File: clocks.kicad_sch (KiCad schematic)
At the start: 17 parts, among them U42 CDCE906PWR, Y5 ABM8G-12.000MHZ-18-D2Y-T, Y6 AX3DCF1-200.0000

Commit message: Loclib
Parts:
- C365, C367: footprint antmicro-footprints:0402-cap -> K410T-devboard-footprints:0402-cap; symbol antmicroCapacitors0402:C_22p_0402 -> K410T-devboard:C_22p_0402
- C366, C373: footprint antmicro-footprints:0201-cap -> K410T-devboard-footprints:0201-cap; symbol antmicroCapacitorsmisc:C_4u7_0201 -> K410T-devboard:C_4u7_0201
- C368, C369, C370, C371, C372: footprint antmicro-footprints:0402-cap -> K410T-devboard-footprints:0402-cap; symbol antmicroCapacitors0402:C_100n_0402 -> K410T-devboard:C_100n_0402
- R334: footprint antmicro-footprints:0402-res -> K410T-devboard-footprints:0402-res; symbol antmicroResistors0402:R_100R_0402 -> K410T-devboard:R_100R_0402
- R335, R336, R337: footprint antmicro-footprints:0402-res -> K410T-devboard-footprints:0402-res; symbol antmicroResistors0402:R_22R_0402 -> K410T-devboard:R_22R_0402
- R352: footprint antmicro-footprints:0402-res -> K410T-devboard-footprints:0402-res; symbol antmicroResistors0402:R_10k_0402 -> K410T-devboard:R_10k_0402
- U42: footprint antmicro-footprints:TSSOP-20_W4.4mm -> K410T-devboard-footprints:TSSOP-20_W4.4mm; symbol antmicroClockTimingClockGeneratorsPLLsFrequencySynthesizers:CDCE906PWR -> K410T-devboard:CDCE906PWR
- Y5: footprint antmicro-footprints:KX-7 -> K410T-devboard-footprints:KX-7; symbol antmicroCrystals:ABM8G-12.000MHZ-18-D2Y-T -> K410T-devboard:ABM8G-12.000MHZ-18-D2Y-T
- Y6: footprint antmicro-footprints:AX3DAF1 -> K410T-devboard-footprints:AX3DAF1; symbol antmicroOscillators:AX3DCF1-200.0000 -> K410T-devboard:AX3DCF1-200.0000

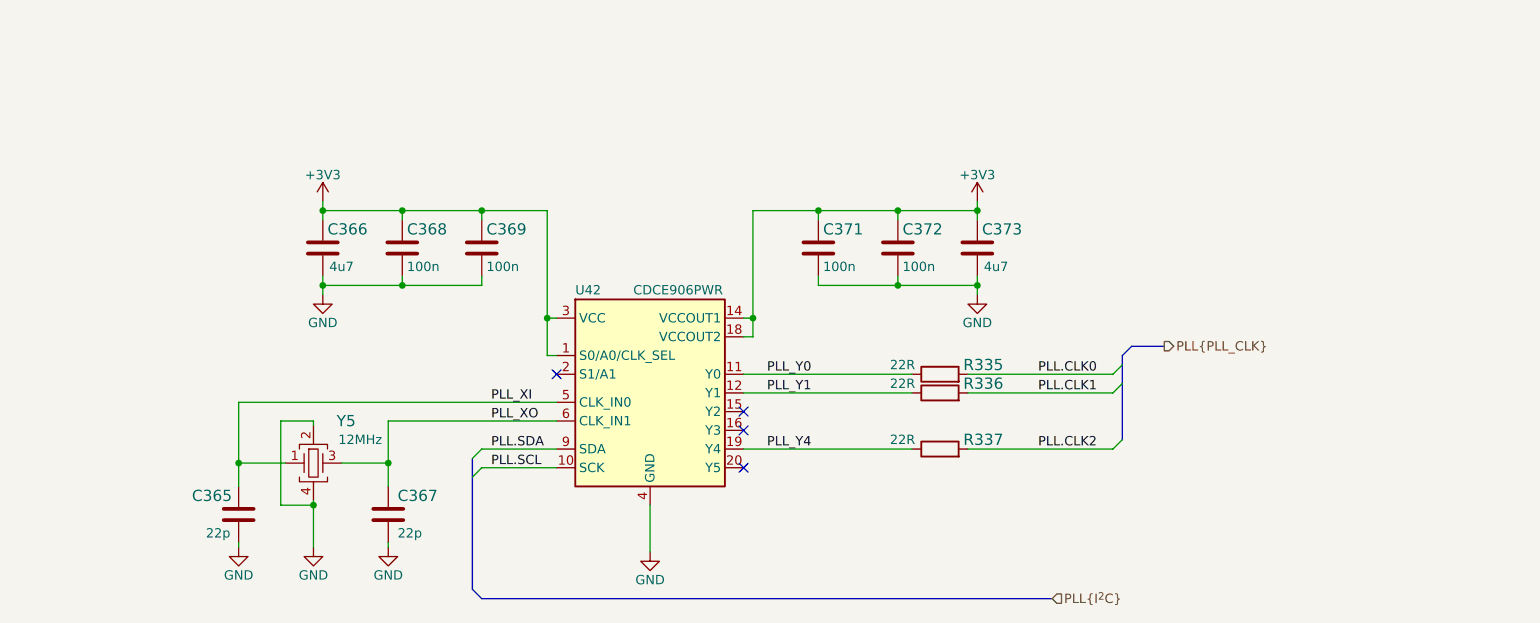
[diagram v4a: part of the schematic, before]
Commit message: Corrected schematic according to review
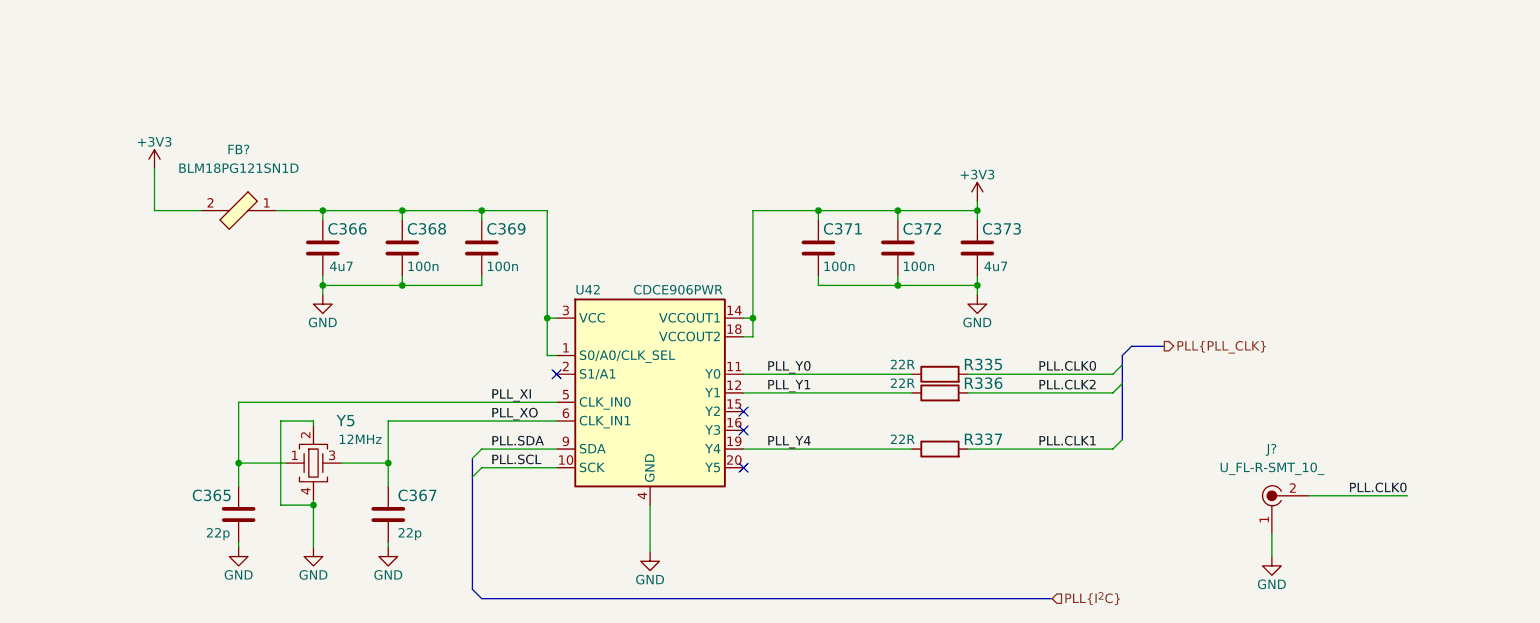
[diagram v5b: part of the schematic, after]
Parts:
- added FB?: BLM18PG121SN1D, K410T-devboard-footprints:0603-res, symbol K410T-devboard:BLM18PG121SN1D
- added J?: U_FL-R-SMT_10_, antmicro-footprints:Coax_Conn_U.FL, symbol antmicroCoaxialConnectorsRF:U_FL-R-SMT_10_
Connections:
- net +3V3: now also FB?.2; no longer C366.1, C368.1, C369.1, U42.1 (S0/A0/CLK_SEL), U42.3 (VCC), U42.7 (VCC)
- net GND: now also J?.1
- net PLL.CLK0: now also J?.2
- net PLL.CLK1: now also R337.2; no longer R336.2
- net PLL.CLK2: now also R336.2; no longer R337.2
- new net: C366.1, C368.1, C369.1, FB?.1, U42.1 (S0/A0/CLK_SEL), U42.3 (VCC), U42.7 (VCC)
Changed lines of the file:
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@@
     (rev "0.0.99")
   )
+  (bus_alias "CLK" (members "CLK_P" "CLK_N"))
+  (bus_alias "I^{2}C" (members "SDA" "SCL"))
   (bus_alias "PLL_CLK" (members "CLK[0..2]"))
-  (bus_alias "I^{2}C" (members "SDA" "SCL"))
-  (bus_alias "CLK" (members "CLK_P" "CLK_N"))
+  (junction (at 176.53 175.895) (diameter 0) (color 0 0 0 0)
+  )
   (junction (at 265.43 175.895) (diameter 0) (color 0 0 0 0)
   )
@@
   )
   (junction (at 254.635 186.055) (diameter 0) (color 0 0 0 0)
-  )
-  (junction (at 176.53 175.895) (diameter 0) (color 0 0 0 0)
   )
   (junction (at 200.025 78.74) (diameter 0) (color 0 0 0 0)
@@
     (stroke (width 0) (type default) (color 0 0 0 0))
   )
+  (wire (pts (xy 305.435 219.71) (xy 305.435 222.885))
+    (stroke (width 0) (type default) (color 0 0 0 0))
+  )
   (wire (pts (xy 265.43 186.055) (xy 254.635 186.055))
     (stroke (width 0) (type default) (color 0 0 0 0))
@@
     (stroke (width 0) (type default) (color 0 0 0 0))
   )
+  (wire (pts (xy 153.67 175.895) (xy 153.67 170.18))
+    (stroke (width 0) (type default) (color 0 0 0 0))
+  )
   (wire (pts (xy 232.41 82.55) (xy 233.68 82.55))
     (stroke (width 0) (type default) (color 0 0 0 0))
@@
     (stroke (width 0) (type default) (color 0 0 0 0))
   )
-  (wire (pts (xy 176.53 177.165) (xy 176.53 175.895))
+  (wire (pts (xy 310.515 214.63) (xy 323.85 214.63))
     (stroke (width 0) (type default) (color 0 0 0 0))
   )
@@
     (stroke (width 0) (type default) (color 0 0 0 0))
   )
+  (wire (pts (xy 160.02 175.895) (xy 153.67 175.895))
+    (stroke (width 0) (type default) (color 0 0 0 0))
+  )
   (wire (pts (xy 231.14 81.28) (xy 232.41 81.28))
     (stroke (width 0) (type default) (color 0 0 0 0))
@@
     (stroke (width 0) (type default) (color 0 0 0 0))
   )
+  (wire (pts (xy 176.53 175.895) (xy 176.53 177.165))
+    (stroke (width 0) (type default) (color 0 0 0 0))
+  )
   (wire (pts (xy 265.43 186.055) (xy 265.43 187.325))
     (stroke (width 0) (type default) (color 0 0 0 0))
@@
     (stroke (width 0) (type default) (color 0 0 0 0))
   )
-  (wire (pts (xy 176.53 174.625) (xy 176.53 175.895))
-    (stroke (width 0) (type default) (color 0 0 0 0))
-  )
   (wire (pts (xy 242.57 82.55) (xy 242.57 78.74))
     (stroke (width 0) (type default) (color 0 0 0 0))
@@
   )
   (wire (pts (xy 194.945 78.74) (xy 200.025 78.74))
+    (stroke (width 0) (type default) (color 0 0 0 0))
+  )
+  (wire (pts (xy 170.18 175.895) (xy 176.53 175.895))
     (stroke (width 0) (type default) (color 0 0 0 0))
   )
@@
     (effects (font (size 1.27 1.27)) (justify left bottom))
   )
-  (label "PLL.CLK2" (at 273.685 208.28 0)
+  (label "PLL.CLK2" (at 273.685 200.66 0)
     (effects (font (size 1.27 1.27)) (justify left bottom))
   )
@@
     (effects (font (size 1.27 1.27)) (justify left bottom))
   )
+  (label "PLL.CLK0" (at 323.85 214.63 180)
+    (effects (font (size 1.27 1.27)) (justify right bottom))
+  )
   (label "PLL_XO" (at 199.39 204.47 0)
     (effects (font (size 1.27 1.27)) (justify left bottom))
@@
     (effects (font (size 1.27 1.27)) (justify left bottom))
   )
-  (label "PLL.CLK1" (at 273.685 200.66 0)
+  (label "PLL.CLK1" (at 273.685 208.28 0)
     (effects (font (size 1.27 1.27)) (justify left bottom))
   )
@@
     (pin "1")
   )
-  (symbol (lib_id "K410T-devboard:+3V3") (at 176.53 174.625 0) (unit 1)
+  (symbol (lib_id "K410T-devboard:+3V3") (at 153.67 170.18 0) (unit 1)
     (in_bom yes) (on_board yes) (fields_autoplaced)
-    (property "Reference" "#PWR0411" (id 0) (at 176.53 178.435 0)
-      (effects (font (size 1.27 1.27)) hide)
-    )
-    (property "Value" "+3V3" (id 1) (at 176.53 171.0492 0))
-    (property "Footprint" "" (id 2) (at 176.53 174.625 0)
-      (effects (font (size 1.27 1.27)) hide)
-    )
-    (property "Datasheet" "" (id 3) (at 176.53 174.625 0)
+    (property "Reference" "#PWR0411" (id 0) (at 153.67 173.99 0)
+      (effects (font (size 1.27 1.27)) hide)
+    )
+    (property "Value" "+3V3" (id 1) (at 153.67 166.6042 0))
+    (property "Footprint" "" (id 2) (at 153.67 170.18 0)
+      (effects (font (size 1.27 1.27)) hide)
+    )
+    (property "Datasheet" "" (id 3) (at 153.67 170.18 0)
       (effects (font (size 1.27 1.27)) hide)
     )
@@
     (pin "2")
   )
+  (symbol (lib_id "antmicroCoaxialConnectorsRF:U_FL-R-SMT_10_") (at 305.435 214.63 0) (unit 1)
+    (in_bom yes) (on_board yes) (fields_autoplaced)
+    (property "Reference" "J?" (id 0) (at 305.4349 208.28 0))
+    (property "Value" "U_FL-R-SMT_10_" (id 1) (at 305.4349 210.82 0))
+    (property "Footprint" "antmicro-footprints:Coax_Conn_U.FL" (id 2) (at 310.515 209.55 0)
+      (effects (font (size 1.524 1.524)) (justify left) hide)
+    )
+    (property "Datasheet" "https://media.digikey.com/pdf/Data%20Sheets/Hirose%20PDFs/UFL%20Series.pdf" (id 3) (at 310.515 207.01 0)
+      (effects (font (size 1.524 1.524)) (justify left) hide)
+    )
+    (property "MPN" "U.FL-R-SMT(10)" (id 4) (at 310.515 201.93 0)
+      (effects (font (size 1.524 1.524)) (justify left) hide)
+    )
+    (property "Manufacturer" "Hirose Electric Co Ltd" (id 5) (at 310.515 186.69 0)
+      (effects (font (size 1.524 1.524)) (justify left) hide)
+    )
+    (pin "1")
+    (pin "2")
+  )
   (symbol (lib_id "K410T-devboard:ABM8G-12.000MHZ-18-D2Y-T ") (at 175.26 210.185 0) (unit 1)
     (in_bom yes) (on_board yes)
@@
     (pin "2")
   )
+  (symbol (lib_id "K410T-devboard:GND") (at 305.435 222.885 0) (unit 1)
+    (in_bom yes) (on_board yes)
+    (property "Reference" "#PWR?" (id 0) (at 305.435 229.235 0)
+      (effects (font (size 1.524 1.524)) hide)
+    )
+    (property "Value" "GND" (id 1) (at 305.435 226.695 0))
+    (property "Footprint" "" (id 2) (at 305.435 222.885 0)
+      (effects (font (size 1.27 1.27)) hide)
+    )
+    (property "Datasheet" "" (id 3) (at 305.435 222.885 0)
+      (effects (font (size 1.27 1.27)) hide)
+    )
+    (pin "1")
+  )
   (symbol (lib_id "K410T-devboard:+1V8") (at 201.93 60.325 0) (unit 1)
     (in_bom yes) (on_board yes) (fields_autoplaced)
@@
     (pin "1")
   )
+  (symbol (lib_id "K410T-devboard:BLM18PG121SN1D") (at 165.1 175.895 0) (mirror y) (unit 1)
+    (in_bom yes) (on_board yes) (fields_autoplaced)
+    (property "Reference" "FB?" (id 0) (at 165.1 167.64 0))
+    (property "Value" "BLM18PG121SN1D" (id 1) (at 165.1 170.18 0))
+    (property "Footprint" "K410T-devboard-footprints:0603-res" (id 2) (at 160.02 170.815 0)
+      (effects (font (size 1.27 1.27)) (justify left) hide)
+    )
+    (property "Datasheet" "https://www.murata.com/en-us/products/productdata/8796738650142/ENFA0003.pdf" (id 3) (at 160.02 168.275 0)
+      (effects (font (size 1.27 1.27)) (justify left) hide)
+    )
+    (property "MPN" "BLM18PG121SN1D" (id 4) (at 160.02 163.195 0)
+      (effects (font (size 1.27 1.27)) (justify left) hide)
+    )
+    (property "Manufacturer" "Murata Electronics North America" (id 5) (at 160.02 147.955 0)
+      (effects (font (size 1.27 1.27)) (justify left) hide)
+    )
+    (pin "1")
+    (pin "2")
+  )
   (symbol (lib_id "K410T-devboard:CDCE906PWR") (at 220.98 200.66 0) (unit 1)

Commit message: Finished implementing all changes from sch review
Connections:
- net at C366.1, C368.1, C369.1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: no longer U42.1 (S0/A0/CLK_SEL)
- new net SUP_MCU.PG_3V3: U42.1 (S0/A0/CLK_SEL)
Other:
- note removed: "Todo: -connect S0 to 3V3 PG ?"
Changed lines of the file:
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@@
   (junction (at 243.84 175.895) (diameter 0) (color 0 0 0 0)
-  )
-  (junction (at 207.01 190.5) (diameter 0) (color 0 0 0 0)
   )
   (junction (at 187.325 175.895) (diameter 0) (color 0 0 0 0)
@@
     (stroke (width 0) (type default) (color 0 0 0 0))
   )
+  (bus_entry (at 187.96 195.58) (size 1.27 0)
+    (stroke (width 0) (type default) (color 0 0 0 0))
+  )
   (bus_entry (at 257.81 73.66) (size -2.54 2.54)
     (stroke (width 0) (type default) (color 0 0 0 0))
@@
     (stroke (width 0) (type default) (color 0 0 0 0))
   )
-  (wire (pts (xy 207.01 195.58) (xy 207.01 190.5))
+  (bus (pts (xy 186.69 195.58) (xy 187.96 195.58))
     (stroke (width 0) (type default) (color 0 0 0 0))
   )
@@
     (stroke (width 0) (type default) (color 0 0 0 0))
   )
-  (wire (pts (xy 208.28 195.58) (xy 207.01 195.58))
+  (wire (pts (xy 189.23 195.58) (xy 208.28 195.58))
     (stroke (width 0) (type default) (color 0 0 0 0))
   )
@@
     (effects (font (size 1.27 1.27) (thickness 0.254) bold) (justify left bottom))
   )
-  (text "Todo:\n-connect S0 to 3V3 PG ?" (at 1.27 8.89 0)
-    (effects (font (size 1.27 1.27)) (justify left bottom))
-  )
   (label "PLL_XI" (at 199.39 201.93 0)
     (effects (font (size 1.27 1.27)) (justify left bottom))
@@
     (effects (font (size 1.27 1.27)) (justify left bottom))
   )
+  (label "SUP_MCU.PG_3V3" (at 205.74 195.58 180)
+    (effects (font (size 1.27 1.27)) (justify right bottom))
+  )
   (label "PLL.CLK1" (at 273.685 208.28 0)
     (effects (font (size 1.27 1.27)) (justify left bottom))
@@
     (effects (font (size 1.27 1.27)) (justify left))
   )
+  (hierarchical_label "SUP_MCU{SUP-MCU}" (shape bidirectional) (at 186.69 195.58 180)
+    (effects (font (size 1.27 1.27)) (justify right))
+  )
   (hierarchical_label "SYS{CLK}" (shape output) (at 275.59 71.12 0)

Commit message: Updated annotation
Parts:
- gave numbers to parts that had none: 2
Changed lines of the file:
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@@
     (rev "0.0.99")
   )
+  (bus_alias "CLK" (members "CLK_P" "CLK_N"))
+  (bus_alias "I^{2}C" (members "SDA" "SCL"))
   (bus_alias "PLL_CLK" (members "CLK[0..2]"))
-  (bus_alias "I^{2}C" (members "SDA" "SCL"))
-  (bus_alias "CLK" (members "CLK_P" "CLK_N"))
   (junction (at 176.53 175.895) (diameter 0) (color 0 0 0 0)
   )
@@
   (symbol (lib_id "antmicroCoaxialConnectorsRF:U_FL-R-SMT_10_") (at 305.435 214.63 0) (unit 1)
     (in_bom yes) (on_board yes) (fields_autoplaced)
-    (property "Reference" "J?" (id 0) (at 305.4349 208.28 0))
+    (property "Reference" "J3" (id 0) (at 305.4349 208.28 0))
     (property "Value" "U_FL-R-SMT_10_" (id 1) (at 305.4349 210.82 0))
     (property "Footprint" "antmicro-footprints:Coax_Conn_U.FL" (id 2) (at 310.515 209.55 0)
@@
   (symbol (lib_id "K410T-devboard:GND") (at 305.435 222.885 0) (unit 1)
     (in_bom yes) (on_board yes)
-    (property "Reference" "#PWR?" (id 0) (at 305.435 229.235 0)
+    (property "Reference" "#PWR0503" (id 0) (at 305.435 229.235 0)
       (effects (font (size 1.524 1.524)) hide)
     )
@@
   (symbol (lib_id "K410T-devboard:BLM18PG121SN1D") (at 165.1 175.895 0) (mirror y) (unit 1)
     (in_bom yes) (on_board yes) (fields_autoplaced)
-    (property "Reference" "FB?" (id 0) (at 165.1 167.64 0))
+    (property "Reference" "FB12" (id 0) (at 165.1 167.64 0))
     (property "Value" "BLM18PG121SN1D" (id 1) (at 165.1 170.18 0))
     (property "Footprint" "K410T-devboard-footprints:0603-res" (id 2) (at 160.02 170.815 0)
